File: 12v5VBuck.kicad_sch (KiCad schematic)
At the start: 14 parts, among them IC1 TPS54302DDCT

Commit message: updated schematic
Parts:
- added J1: Conn_01x02, Connector_PinHeader_2.54mm:PinHeader_1x02_P2.54mm_Vertical, symbol Connector_Generic:Conn_01x02
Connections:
- net +12V: now also J1.1 (Pin_1)
- net GND: now also J1.2 (Pin_2)
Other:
- note added: "12v to 5V"
- note added: "INPUT"
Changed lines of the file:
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@@
   (junction (at 158.75 70.485) (diameter 0) (color 0 0 0 0)
   )
+  (wire (pts (xy 64.77 73.025) (xy 64.77 74.93))
+    (stroke (width 0) (type default))
+  )
   (wire (pts (xy 193.675 88.265) (xy 193.675 89.535))
     (stroke (width 0) (type default))
@@
     (stroke (width 0) (type default))
   )
+  (wire (pts (xy 66.675 73.025) (xy 64.77 73.025))
+    (stroke (width 0) (type default))
+  )
   (wire (pts (xy 123.19 75.565) (xy 129.54 75.565))
     (stroke (width 0) (type default))
@@
     (stroke (width 0) (type default))
   )
+  (wire (pts (xy 66.675 70.485) (xy 64.77 70.485))
+    (stroke (width 0) (type default))
+  )
   (wire (pts (xy 106.045 65.405) (xy 106.045 62.865))
     (stroke (width 0) (type default))
@@
     (stroke (width 0) (type default))
   )
+  (wire (pts (xy 64.77 67.31) (xy 64.77 70.485))
+    (stroke (width 0) (type default))
+  )
   (wire (pts (xy 165.1 75.565) (xy 165.1 83.185))
     (stroke (width 0) (type default))
@@
     (stroke (width 0) (type default))
   )
+  (rectangle (start 55.88 60.325) (end 80.645 83.185)
+    (stroke (width 0) (type default))
+    (fill (type none))
+  )
+  (rectangle (start 102.87 57.15) (end 201.93 94.615)
+    (stroke (width 0) (type default))
+    (fill (type none))
+  )
+  (text "12v to 5V" (at 136.525 56.515 0)
+    (effects (font (size 4 4)) (justify left bottom))
+  )
+  (text "INPUT" (at 59.69 59.69 0)
+    (effects (font (size 3 3)) (justify left bottom))
+  )
   (symbol (lib_id "power:GND") (at 177.165 75.565 0) (unit 1)
     (in_bom yes) (on_board yes) (dnp no)
@@
         (path "/5b52d536-76f3-4180-b70d-b6911106f62c"
           (reference "#PWR06") (unit 1)
+        )
+      )
+    )
+  )
+  (symbol (lib_id "power:+12V") (at 64.77 67.31 0) (unit 1)
+    (in_bom yes) (on_board yes) (dnp no) (fields_autoplaced)
+    (property "Reference" "#PWR09" (at 64.77 71.12 0)
+      (effects (font (size 1.27 1.27)) hide)
+    )
+    (property "Value" "+12V" (at 64.77 62.865 0)
+      (effects (font (size 1.27 1.27)))
+    )
+    (property "Footprint" "" (at 64.77 67.31 0)
+      (effects (font (size 1.27 1.27)) hide)
+    )
+    (property "Datasheet" "" (at 64.77 67.31 0)
+      (effects (font (size 1.27 1.27)) hide)
+    )
+    (pin "1")
+    (instances
+      (project "12v5VBuck"
+        (path "/5b52d536-76f3-4180-b70d-b6911106f62c"
+          (reference "#PWR09") (unit 1)
         )
       )
@@
     )
   )
+  (symbol (lib_id "power:GND") (at 64.77 74.93 0) (unit 1)
+    (in_bom yes) (on_board yes) (dnp no)
+    (property "Reference" "#PWR010" (at 64.77 81.28 0)
+      (effects (font (size 1.27 1.27)) hide)
+    )
+    (property "Value" "GND" (at 64.77 78.105 0)
+      (effects (font (size 1.27 1.27)))
+    )
+    (property "Footprint" "" (at 64.77 74.93 0)
+      (effects (font (size 1.27 1.27)) hide)
+    )
+    (property "Datasheet" "" (at 64.77 74.93 0)
+      (effects (font (size 1.27 1.27)) hide)
+    )
+    (pin "1")
+    (instances
+      (project "12v5VBuck"
+        (path "/5b52d536-76f3-4180-b70d-b6911106f62c"
+          (reference "#PWR010") (unit 1)
+        )
+      )
+    )
+  )
   (symbol (lib_id "power:GND") (at 127 71.12 0) (unit 1)
     (in_bom yes) (on_board yes) (dnp no)
@@
         (path "/5b52d536-76f3-4180-b70d-b6911106f62c"
           (reference "#PWR05") (unit 1)
+        )
+      )
+    )
+  )
+  (symbol (lib_id "Connector_Generic:Conn_01x02") (at 71.755 70.485 0) (unit 1)
+    (in_bom yes) (on_board yes) (dnp no)
+    (property "Reference" "J1" (at 70.485 67.945 0)
+      (effects (font (size 1.27 1.27)) (justify left))
+    )
+    (property "Value" "Conn_01x02" (at 74.93 73.025 0)
+      (effects (font (size 1.27 1.27)) (justify left) hide)
+    )
+    (property "Footprint" "Connector_PinHeader_2.54mm:PinHeader_1x02_P2.54mm_Vertical" (at 71.755 70.485 0)
+      (effects (font (size 1.27 1.27)) hide)
+    )
+    (property "Datasheet" "~" (at 71.755 70.485 0)
+      (effects (font (size 1.27 1.27)) hide)
+    )
+    (pin "1")
+    (pin "2")
+    (instances
+      (project "12v5VBuck"
+        (path "/5b52d536-76f3-4180-b70d-b6911106f62c"
+          (reference "J1") (unit 1)
         )
       )
@@
   )
   (symbol (lib_id "TPS54302DDCT:TPS54302DDCT") (at 129.54 65.405 0) (unit 1)
-    (in_bom yes) (on_board yes) (dnp no) (fields_autoplaced)
-    (property "Reference" "IC1" (at 143.51 58.42 0)
-      (effects (font (size 1.27 1.27)))
-    )
-    (property "Value" "TPS54302DDCT" (at 143.51 60.96 0)
-      (effects (font (size 1.27 1.27)))
-    )
+    (in_bom yes) (on_board yes) (dnp no)
+    (property "Reference" "IC1" (at 140.97 61.595 0)
+      (effects (font (size 1.27 1.27)))
+    )
+    (property "Value" "TPS54302DDCT" (at 140.97 79.375 0)
+      (effects (font (size 1.27 1.27)))
+    )

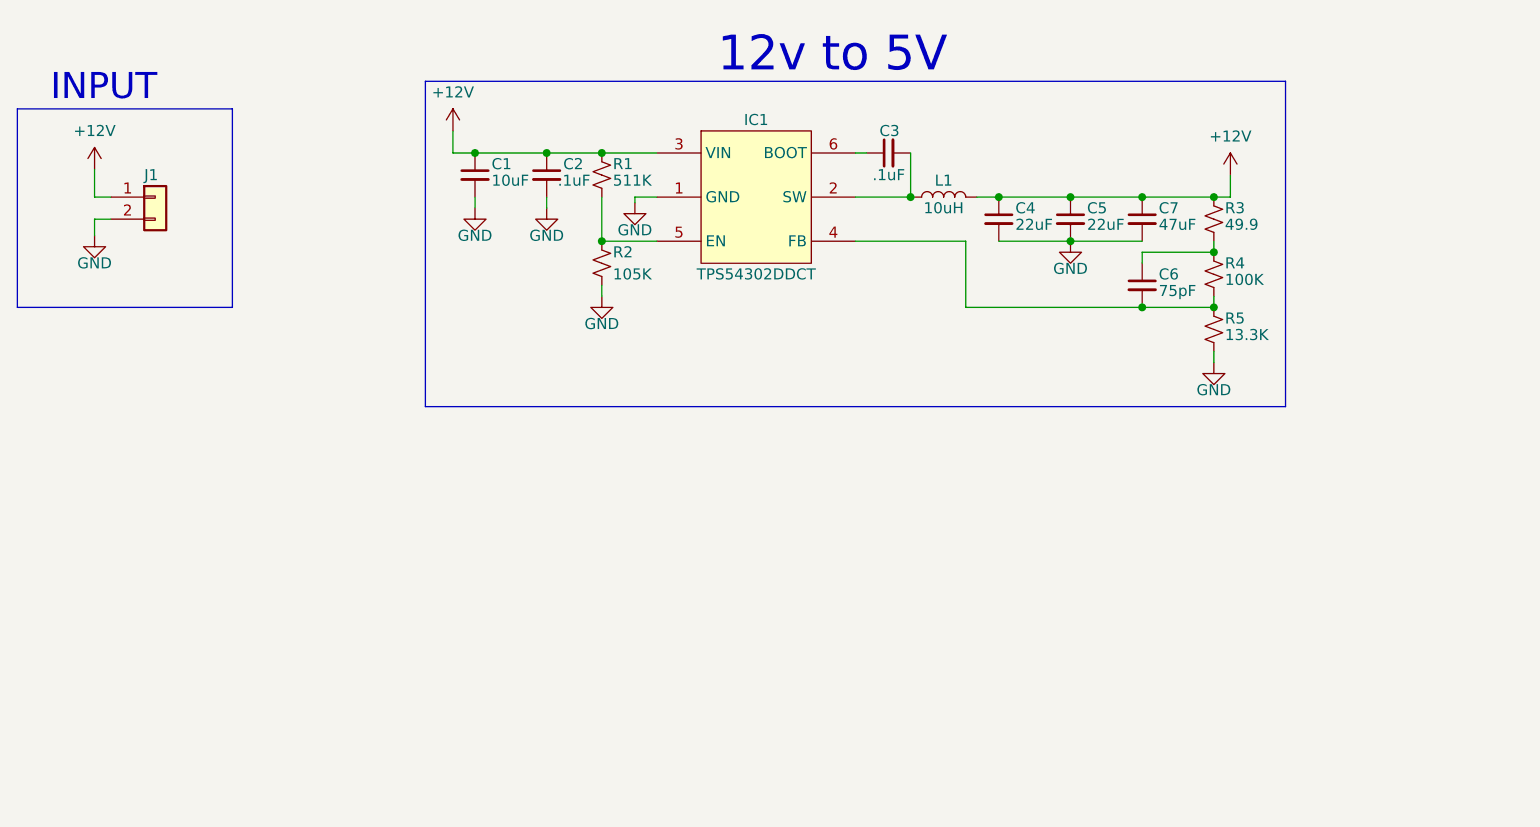
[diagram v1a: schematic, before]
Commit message: Added first buck convertor
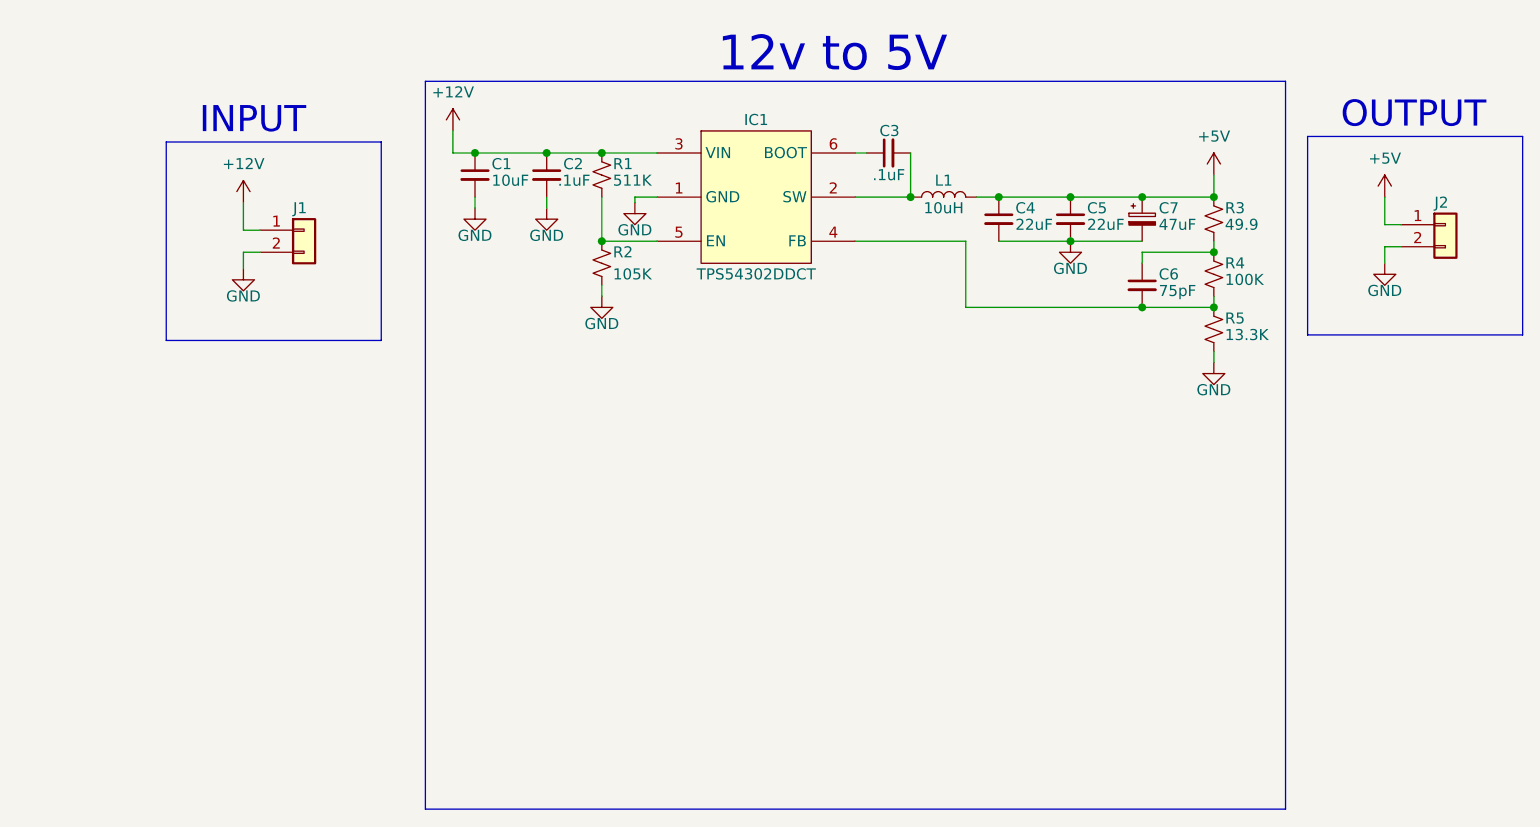
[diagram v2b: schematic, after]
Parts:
- added J2: Conn_01x02, footprints:CONN_1984617_PXC, symbol Connector_Generic:Conn_01x02
- C1, C2, C3, C4, C5, C6: footprint (none) -> Capacitor_SMD:C_0805_2012Metric
- C7: footprint (none) -> Capacitor_THT:C_Radial_D6.3mm_H11.0mm_P2.50mm; symbol Device:C_Small -> Device:C_Polarized_Small
- J1: footprint Connector_PinHeader_2.54mm:PinHeader_1x02_P2.54mm_Vertical -> footprints:CONN_1984617_PXC
- L1: footprint (none) -> Inductor_SMD:L_Abracon_ASPI-0630LR
- R1, R2, R3, R4, R5: footprint (none) -> Resistor_SMD:R_0805_2012Metric
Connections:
- net +12V: no longer C4.1, C5.1, C7.1, L1.2, R3.1
- net GND: now also J2.2 (Pin_2)
- new net +5V: C4.1, C5.1, C7.1, J2.1 (Pin_1), L1.2, R3.1
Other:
- note added: "OUTPUT"
- moved on the sheet: J1

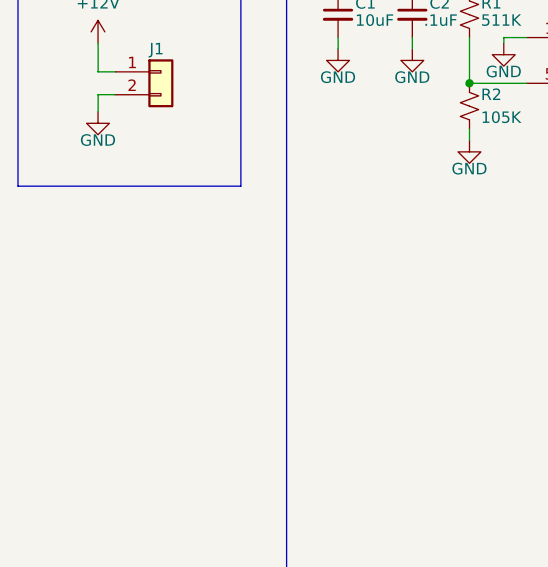
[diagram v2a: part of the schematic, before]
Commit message: Added a mounting hole
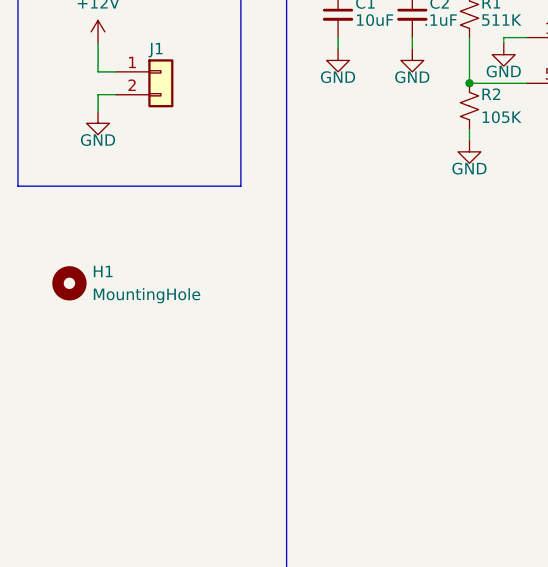
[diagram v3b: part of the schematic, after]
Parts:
- added H1: MountingHole, MountingHole:MountingHole_2.5mm, symbol Mechanical:MountingHole
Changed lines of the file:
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@@
+    )
+  )
+  (symbol (lib_id "Mechanical:MountingHole") (at 78.74 97.79 0) (unit 1)
+    (in_bom yes) (on_board yes) (dnp no) (fields_autoplaced)
+    (property "Reference" "H1" (at 81.28 96.52 0)
+      (effects (font (size 1.27 1.27)) (justify left))
+    )
+    (property "Value" "MountingHole" (at 81.28 99.06 0)
+      (effects (font (size 1.27 1.27)) (justify left))
+    )
+    (property "Footprint" "MountingHole:MountingHole_2.5mm" (at 78.74 97.79 0)
+      (effects (font (size 1.27 1.27)) hide)
+    )
+    (property "Datasheet" "~" (at 78.74 97.79 0)
+      (effects (font (size 1.27 1.27)) hide)
+    )
+    (instances
+      (project "12v5VBuck"
+        (path "/5b52d536-76f3-4180-b70d-b6911106f62c"
+          (reference "H1") (unit 1)
+        )
+      )
     )
   )

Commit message: Updated schematic
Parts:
- C7: footprint Capacitor_THT:C_Radial_D6.3mm_H11.0mm_P2.50mm -> footprints:CAPPM3216X180N
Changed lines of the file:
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@@
       (effects (font (size 1.27 1.27)) (justify left))
     )
-    (property "Footprint" "Capacitor_THT:C_Radial_D6.3mm_H11.0mm_P2.50mm" (at 185.42 73.025 0)
+    (property "Footprint" "footprints:CAPPM3216X180N" (at 185.42 73.025 0)
       (effects (font (size 1.27 1.27)) hide)
     )
